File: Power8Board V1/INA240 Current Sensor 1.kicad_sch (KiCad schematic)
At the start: 3 parts, among them U4 INA240A2PWR

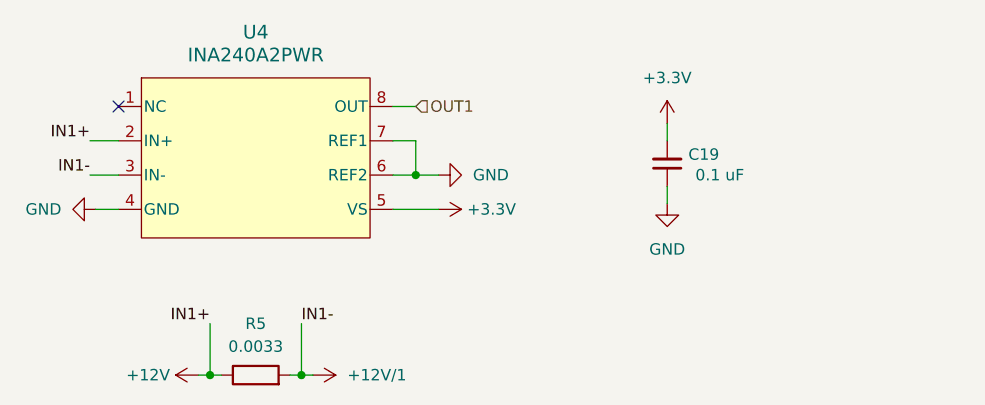
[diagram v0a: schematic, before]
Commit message: Laid out components
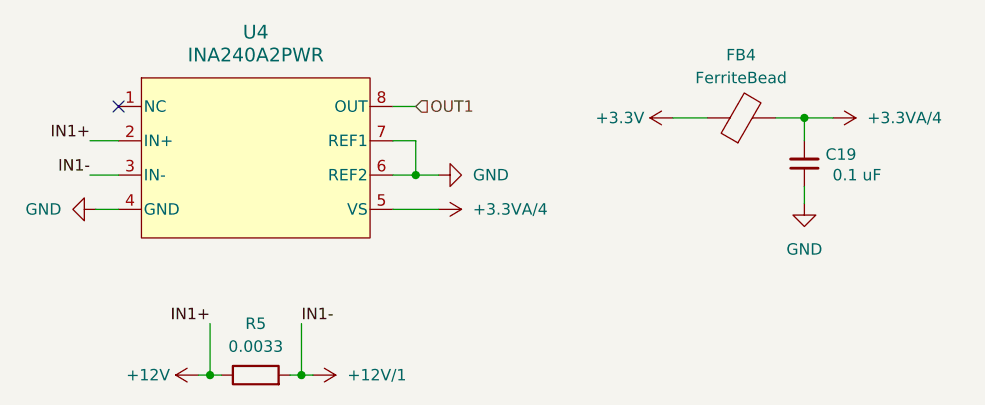
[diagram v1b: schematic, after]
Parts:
- added FB4: FerriteBead, MPZ2012S102ATD25:BEADC2012X105N, symbol Device:FerriteBead
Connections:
- net +3.3V: now also FB4.1; no longer C19.2, U4.5 (VS)
- new net +3.3VA/4: C19.2, FB4.2, U4.5 (VS)
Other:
- moved on the sheet: C19

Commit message: DRC sorted out.
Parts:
- renumbered R5 to R25
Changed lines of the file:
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@@
 		(dnp no)
 		(fields_autoplaced yes)
-		(property "Reference" "R5"
-			(at 140.335 111.125 90)
+		(property "Reference" "R25"
+			(at 140.335 110.49 90)
 			(effects
 				(font
@@
 		)
 		(property "Value" "0.0033"
-			(at 140.335 113.665 90)
+			(at 140.335 113.03 90)
 			(effects
 				(font
@@
 			(project "Power8Board V1"
 				(path "/835b92cb-5206-4b93-b4be-2a785f4797f4/64832d79-2054-4fdb-82f6-de66896e6610/db9137a7-4e97-40ba-b5e6-2da12e50f672"
-					(reference "R5")
+					(reference "R25")
 					(unit 1)
 				)
